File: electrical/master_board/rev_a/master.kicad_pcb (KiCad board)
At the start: 2 copper layers, 144.3 x 156 mm, 0 parts

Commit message: Finally have everything fitting together.
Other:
- outline, holes or cut-outs redrawn

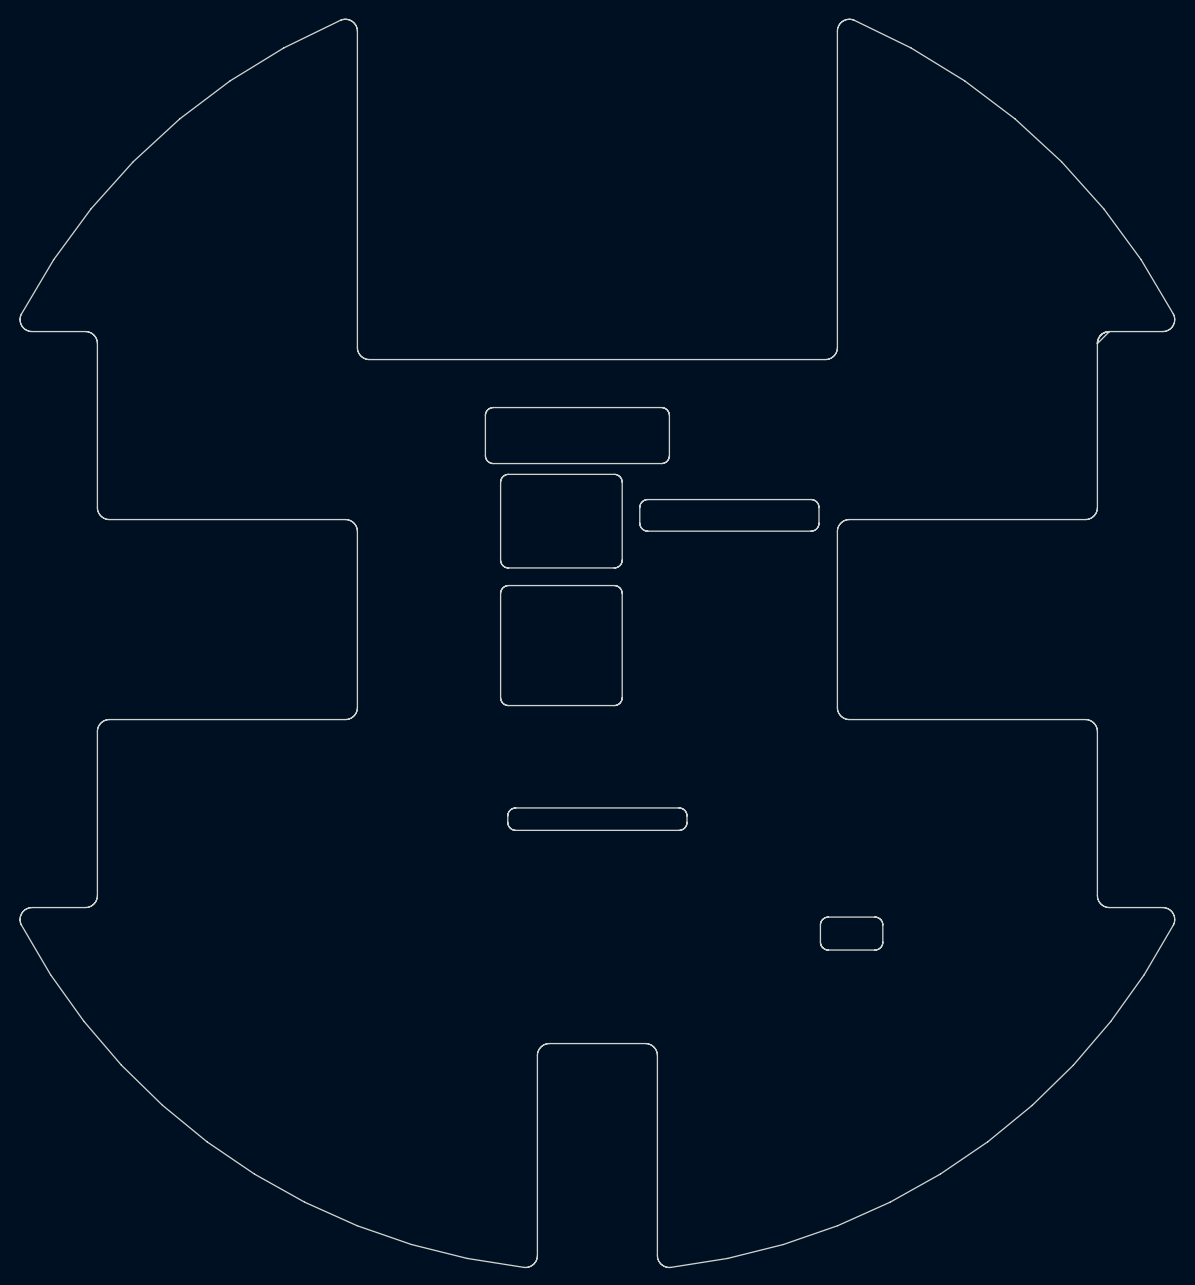
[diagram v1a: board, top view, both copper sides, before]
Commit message: Added spacer mounting holes to schematics and associated PCB's.
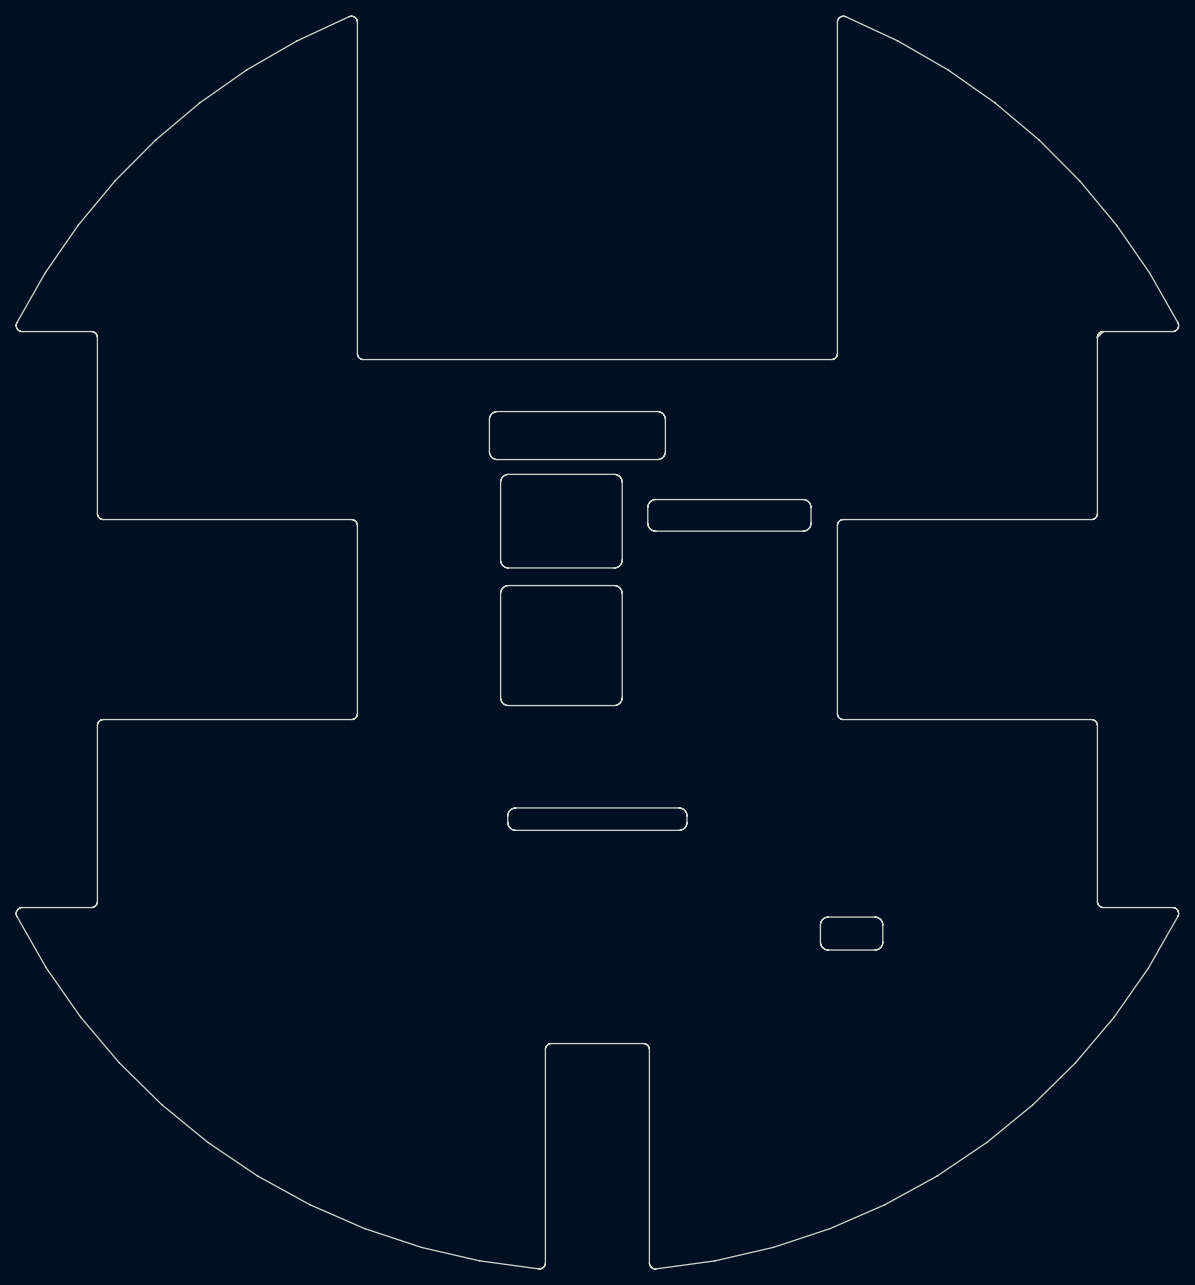
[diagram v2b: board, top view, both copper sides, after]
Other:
- board size 144.3 x 156 mm -> 145.3 x 156.6 mm

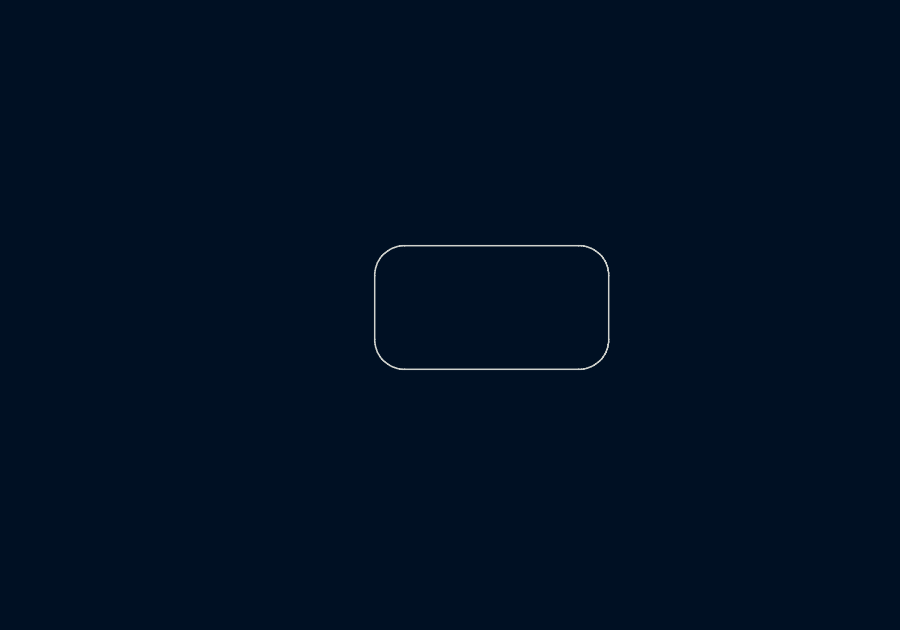
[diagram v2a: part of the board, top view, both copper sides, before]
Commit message: Got the NUCLEO placed. Readjusted a few other parts.
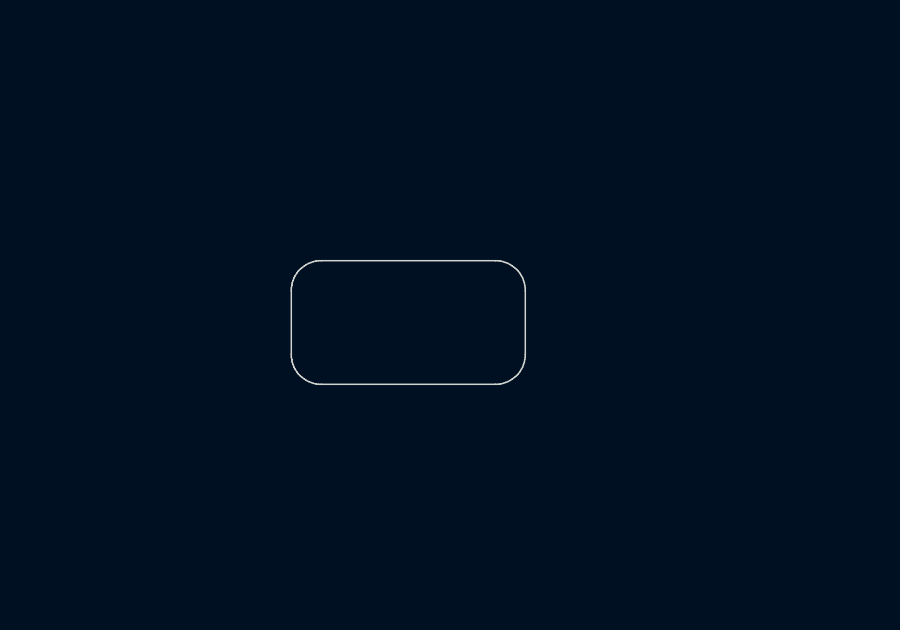
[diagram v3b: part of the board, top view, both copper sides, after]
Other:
- outline, holes or cut-outs redrawn
